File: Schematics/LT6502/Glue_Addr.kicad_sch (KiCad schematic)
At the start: 31 parts, among them IC1 ATF1508AS-7AX100, J1 Conn_02x05_Odd_Even, J15 Conn_01x06, J16 Conn_01x03, J18 Conn_01x03, X1 28.322MHz, Y1 ECS-P55-28.000MHZ-AN

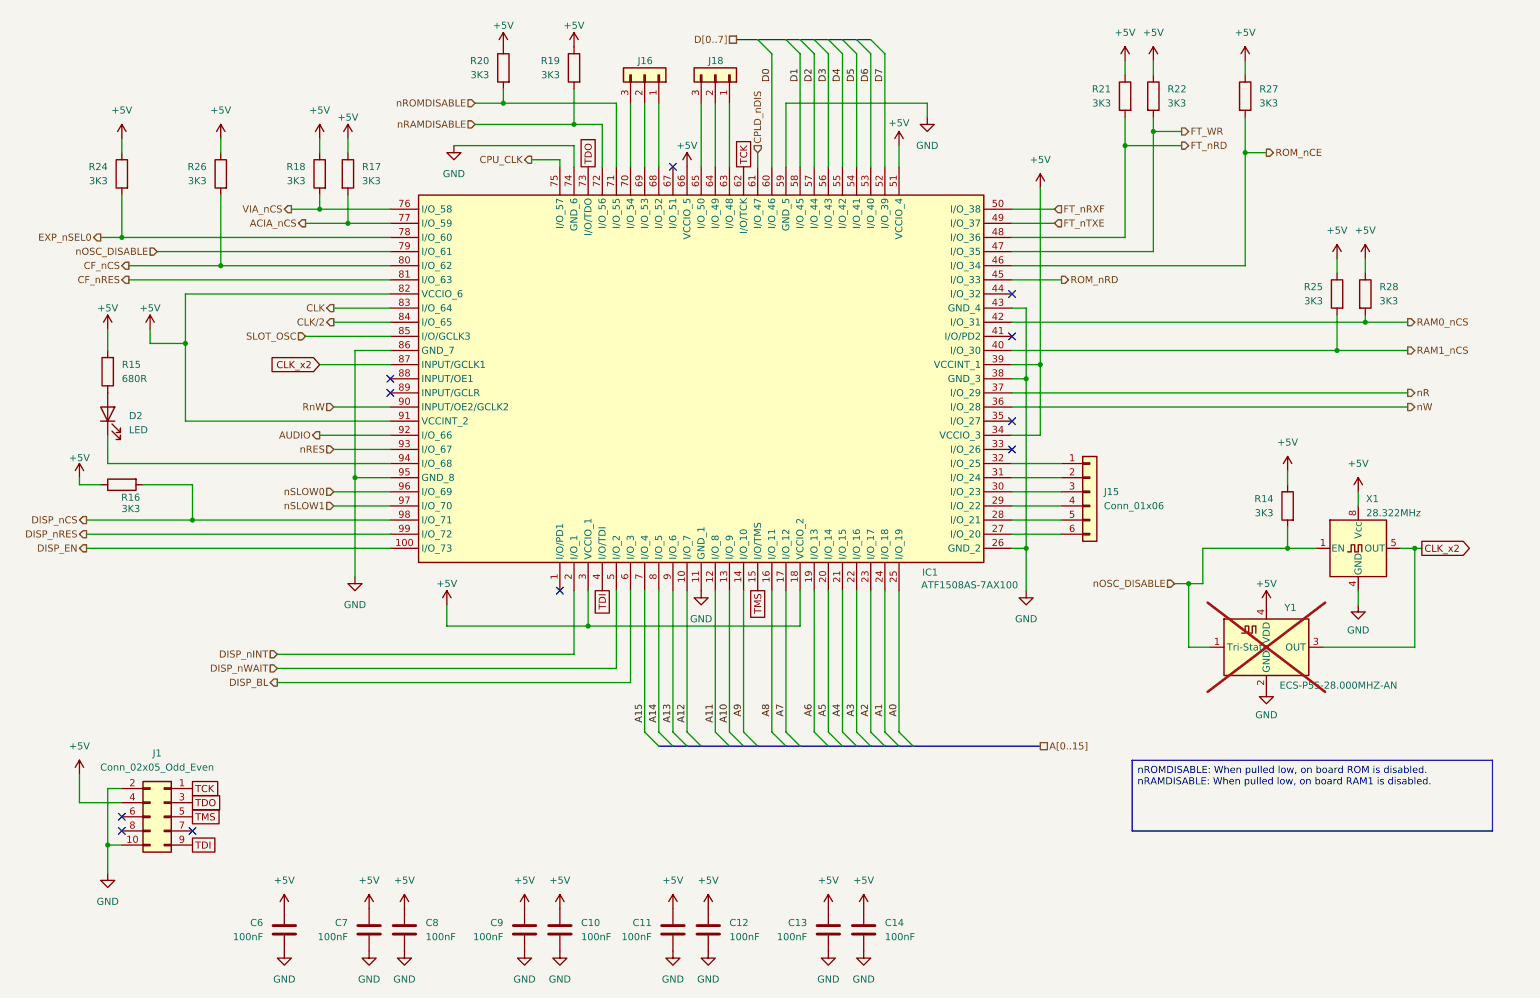
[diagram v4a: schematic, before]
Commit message: Updated BoMs ordered PCBs
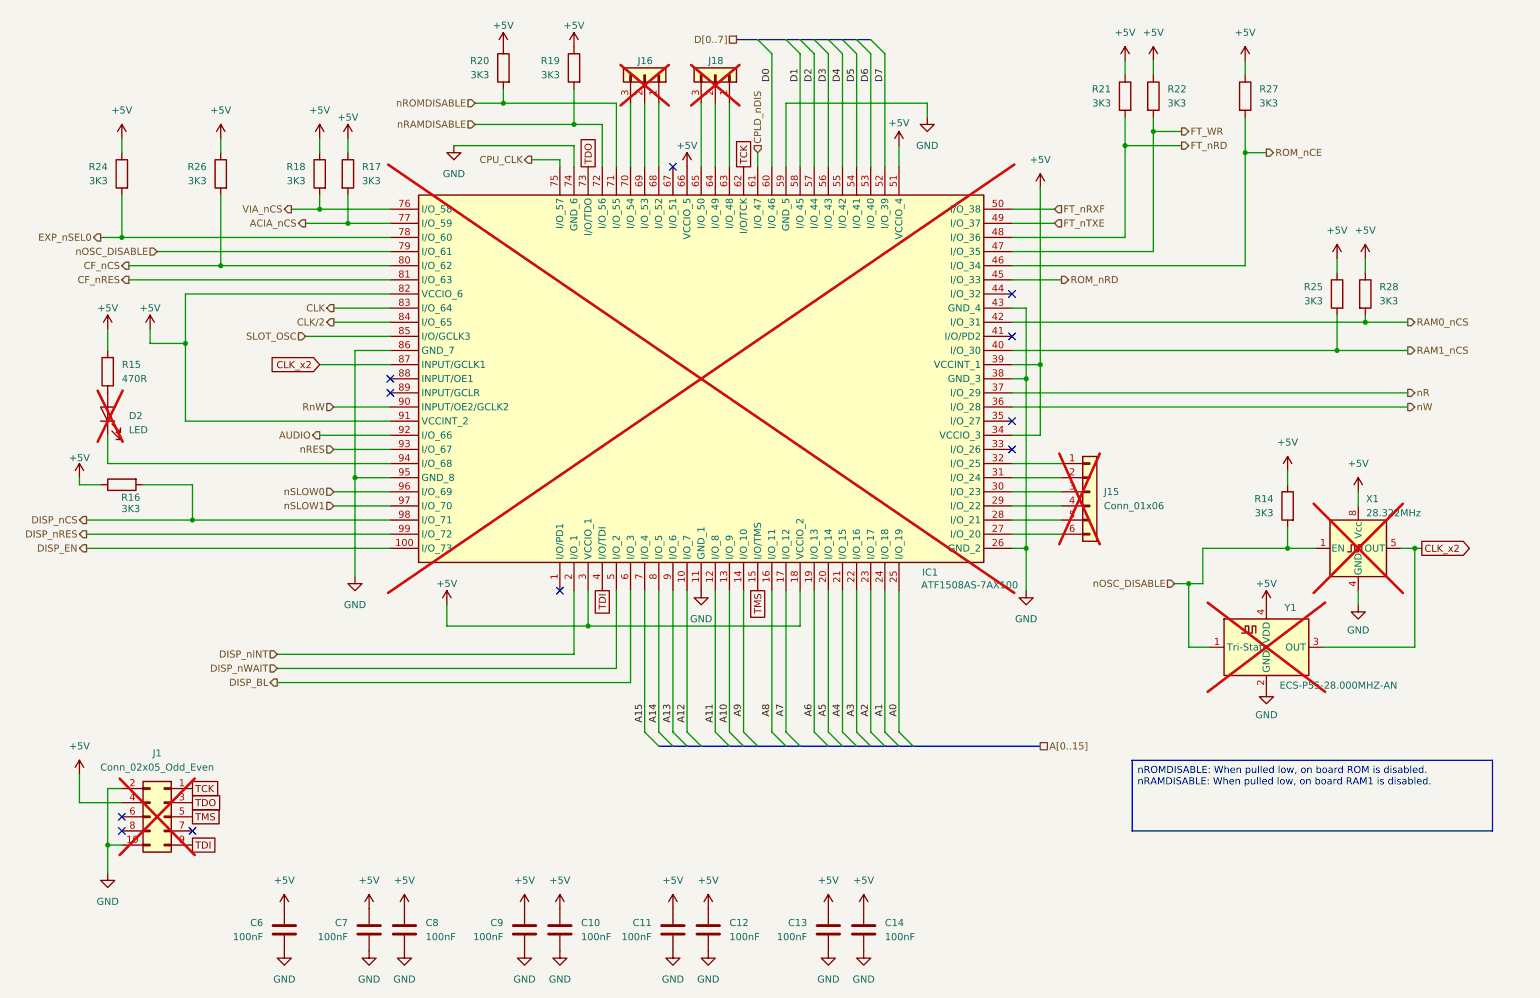
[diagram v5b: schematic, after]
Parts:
- C10: LCSC C49678 -> C1581
- C11, C12, C13, C14, C6, C7, C8, C9: LCSC C49678 -> C113803
- D2, IC1, J15, J16, J18: LCSC (none) -> DNF; now not fitted
- J1, X1: now not fitted
- R15: value 680R -> 470R; LCSC C23179 -> C25117
- R16, R17, R18, R19, R20, R21, R22, R24, R25, R26, R27, R28: LCSC DNF -> C25890
- Y1: LCSC (none) -> DNF
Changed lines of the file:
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@@
 			)
 		)
-		(property "LCSC" "C49678"
+		(property "LCSC" "C113803"
 			(at 138.43 182.88 0)
 			(effects
@@
 			)
 		)
-		(property "LCSC" "DNF"
+		(property "LCSC" "C25890"
 			(at 251.46 68.58 0)
 			(effects
@@
 		(in_bom yes)
 		(on_board yes)
-		(dnp no)
+		(dnp yes)
 		(property "Reference" "J16"
 			(at 125.73 26.67 90)
@@
 			)
 		)
+		(property "LCSC" "DNF"
+			(at 127 29.21 90)
+			(effects
+				(font
+					(size 1.27 1.27)
+				)
+				(hide yes)
+			)
+		)
 		(pin "2"
 		)
@@
 			)
 		)
+		(property "LCSC" "DNF"
+			(at 238.76 132.08 0)
+			(effects
+				(font
+					(size 1.27 1.27)
+				)
+				(hide yes)
+			)
+		)
 		(pin "4"
 		)
@@
 			)
 		)
-		(property "LCSC" "DNF"
+		(property "LCSC" "C25890"
 			(at 68.58 46.99 0)
 			(effects
@@
 			)
 		)
-		(property "LCSC" "DNF"
+		(property "LCSC" "C25890"
 			(at 50.8 46.99 0)
 			(effects
@@
 		(in_bom yes)
 		(on_board yes)
-		(dnp no)
+		(dnp yes)
 		(fields_autoplaced yes)
 		(property "Reference" "D2"
@@
 			)
 		)
+		(property "LCSC" "DNF"
+			(at 30.48 90.17 90)
+			(effects
+				(font
+					(size 1.27 1.27)
+				)
+				(hide yes)
+			)
+		)
 		(pin "1"
 		)
@@
 			)
 		)
-		(property "LCSC" "DNF"
+		(property "LCSC" "C25890"
 			(at 101.6 27.94 0)
 			(effects
@@
 		(in_bom yes)
 		(on_board yes)
-		(dnp no)
+		(dnp yes)
 		(property "Reference" "IC1"
 			(at 178.308 118.618 90)
@@
 			)
 		)
+		(property "LCSC" "DNF"
+			(at 111.76 121.92 90)
+			(effects
+				(font
+					(size 1.27 1.27)
+				)
+				(hide yes)
+			)
+		)
 		(pin "52"
 		)
@@
 		(in_bom yes)
 		(on_board yes)
-		(dnp no)
+		(dnp yes)
 		(fields_autoplaced yes)
 		(property "Reference" "J1"
@@
 			)
 		)
-		(property "LCSC" "DNF"
+		(property "LCSC" "C25890"
 			(at 33.02 102.87 0)
 			(effects
@@
 			)
 		)
-		(property "LCSC" "C49678"
+		(property "LCSC" "C113803"
 			(at 132.08 182.88 0)
 			(effects
@@
 			)
 		)
-		(property "LCSC" "C49678"
+		(property "LCSC" "C113803"
 			(at 160.02 182.88 0)
 			(effects
@@
 			)
 		)
-		(property "LCSC" "DNF"
+		(property "LCSC" "C25890"
 			(at 218.44 33.02 0)
 			(effects
@@
 			)
 		)
-		(property "LCSC" "DNF"
+		(property "LCSC" "C25890"
 			(at 73.66 46.99 0)
 			(effects
@@
 			)
 		)
-		(property "LCSC" "C49678"
+		(property "LCSC" "C113803"
 			(at 105.41 182.88 0)
 			(effects
@@
 			)
 		)
-		(property "LCSC" "C49678"
+		(property "LCSC" "C1581"
 			(at 111.76 182.88 0)
 			(effects
@@
 		(in_bom yes)
 		(on_board yes)
-		(dnp no)
+		(dnp yes)
 		(property "Reference" "J18"
 			(at 138.43 26.67 90)
@@
 			)
 		)
+		(property "LCSC" "DNF"
+			(at 139.7 29.21 90)
+			(effects
+				(font
+					(size 1.27 1.27)
+				)
+				(hide yes)
+			)
+		)
 		(pin "2"
 		)
@@
 			)
 		)
-		(property "LCSC" "DNF"
+		(property "LCSC" "C25890"
 			(at 33.02 46.99 0)
 			(effects
@@
 			)
 		)
-		(property "LCSC" "C49678"
+		(property "LCSC" "C113803"
 			(at 77.47 182.88 0)
 			(effects
@@
 		(in_bom yes)
 		(on_board yes)
-		(dnp no)
+		(dnp yes)
 		(fields_autoplaced yes)
 		(property "Reference" "J15"
@@
 			)
 		)
+		(property "LCSC" "DNF"
+			(at 207.01 104.14 0)
+			(effects
+				(font
+					(size 1.27 1.27)
+				)
+				(hide yes)
+			)
+		)
 		(pin "4"
 		)
@@
 			)
 		)
-		(property "LCSC" "C49678"
+		(property "LCSC" "C113803"
 			(at 62.23 182.88 0)
 			(effects
@@
 			)
 		)
-		(property "Value" "680R"
+		(property "Value" "470R"
 			(at 33.02 83.8199 0)
 			(effects
@@
 			)
 		)
-		(property "LCSC" "C23179"
+		(property "LCSC" "C25117"
 			(at 30.48 82.55 90)
 			(effects
@@
 			)
 		)
-		(property "LCSC" "DNF"
+		(property "LCSC" "C25890"
 			(at 213.36 33.02 0)
 			(effects
@@
 			)
 		)
-		(property "LCSC" "C49678"
+		(property "LCSC" "C113803"
 			(at 83.82 182.88 0)
 			(effects
@@
 			)
 		)
-		(property "LCSC" "DNF"
+		(property "LCSC" "C25890"
 			(at 114.3 27.94 0)
 			(effects
@@
 			)
 		)
-		(property "LCSC" "C49678"
+		(property "LCSC" "C113803"
 			(at 166.37 182.88 0)
 			(effects
@@
 			)
 		)
-		(property "LCSC" "DNF"
+		(property "LCSC" "C25890"
 			(at 234.95 33.02 0)
 			(effects
@@
 		(in_bom yes)
 		(on_board yes)
-		(dnp no)
+		(dnp yes)
 		(property "Reference" "X1"
 			(at 257.81 105.41 0)
@@
 			)
 		)
-		(property "LCSC" "DNF"
+		(property "LCSC" "C25890"
 			(at 256.54 68.58 0)
 			(effects

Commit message: Auto stash before merge of "main" and "origin/main"
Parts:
- added R89, R90: 3K3, Resistor_SMD:R_0402_1005Metric, symbol Device:R
- D2, IC1, J1, X1: now fitted
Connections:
- net +5V: now also R89.1, R90.1
- net nSLOW0: now also R90.2
- net nSLOW1: now also R89.2

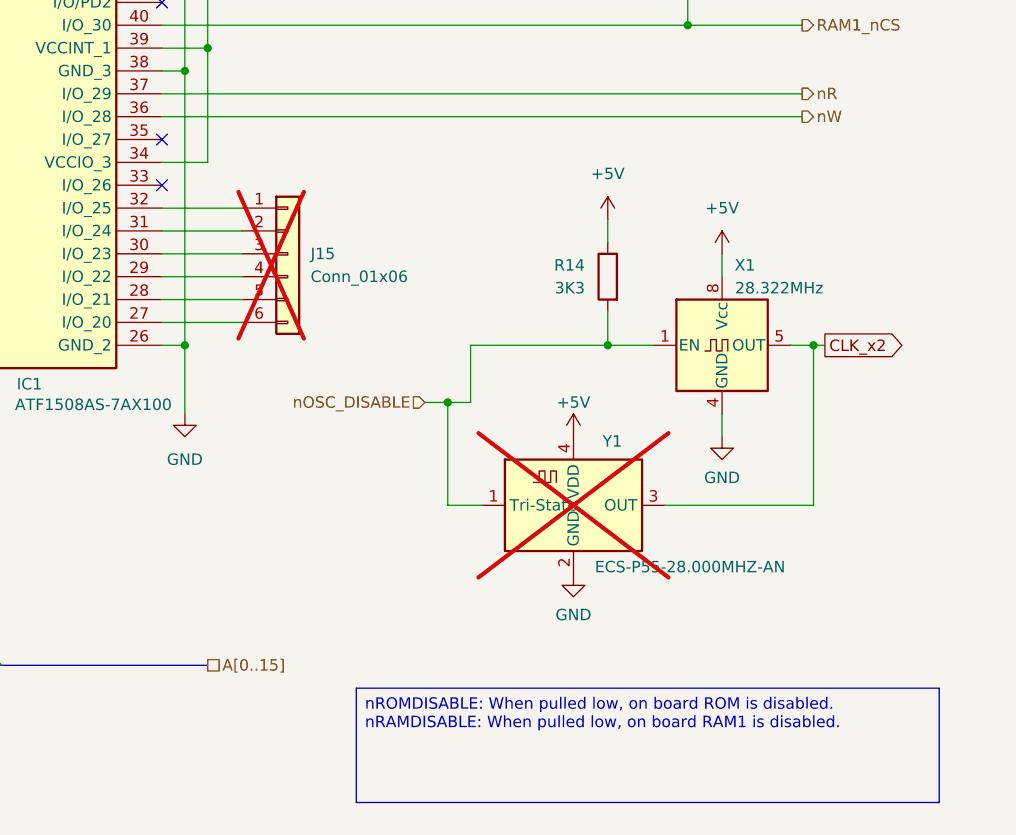
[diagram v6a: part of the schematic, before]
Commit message: Added enable for TXS0108 on data bus
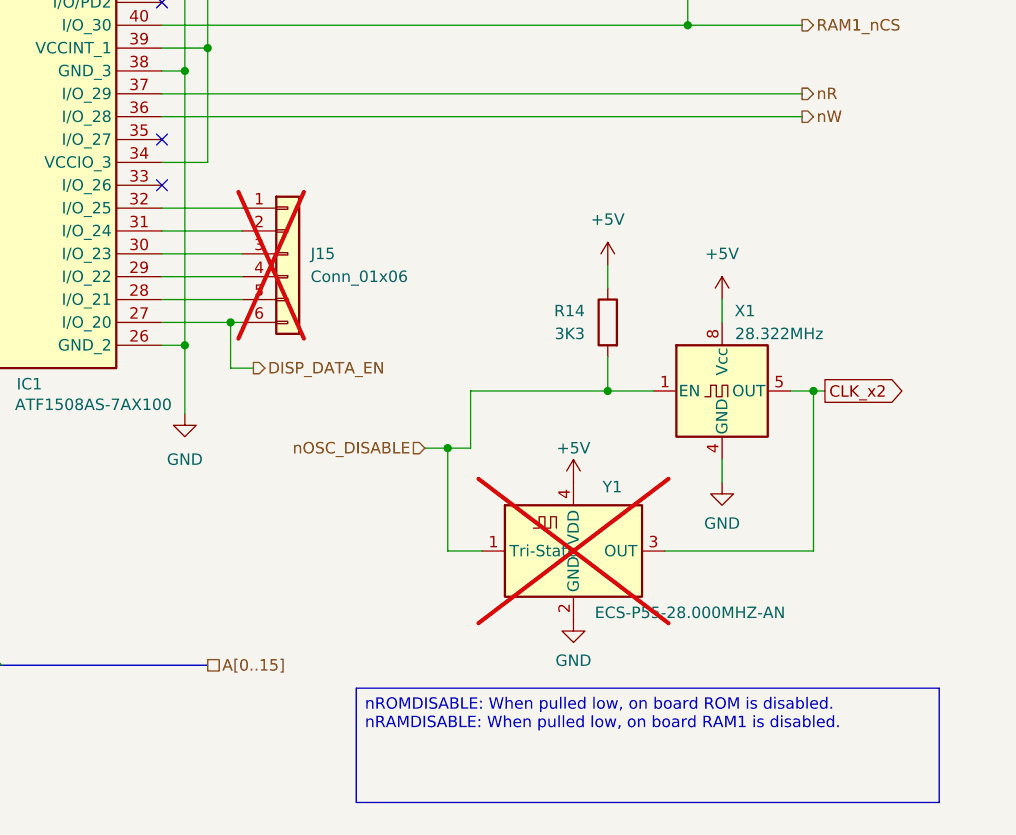
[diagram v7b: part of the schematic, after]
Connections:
- net DISP_DATA_EN: now reaches IC1.27 (I/O_20), J15.6 (Pin_6)
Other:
- moved on the sheet: R14, X1, Y1

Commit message: PCB/Schematic edits
moved speaker hole a little
made nRES resistor for display no fit (this upsets them for some reason)
Added diodes to ensure USB Console chip is powered when nothing attached (this causes issues with booting.
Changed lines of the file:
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@@
+	(wire
+		(pts
+			(xy 193.04 106.68) (xy 201.93 106.68)
+		)
+		(stroke
+			(width 0)
+			(type default)
+		)
+	)
 	(wire
 		(pts
@@
 		)
 		(stroke
-			(width 0)
-			(type default)
-		)
-	)
-	(wire
-		(pts
-			(xy 201.93 106.68) (xy 193.04 106.68)
-		)
-		(stroke
